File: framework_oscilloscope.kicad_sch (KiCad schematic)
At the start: 86 parts, among them IC1 FT232HL-REEL, IC10 93LC56BT-I_OT, IC2 ICE40UP5K-SG48I, IC3 ADC08060CIMTX_NOPB, IC7 OPA356AIDBVR, IC8 TLV77312PDBVR, IC9 LM4040C20IDBZT, J1 BNC, P1 USB_C_Plug_USB2.0, U9 TPS62A02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

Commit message: added part numbers for passives
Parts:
- C10, C12, C14, C15, C17, C18, C19, C21, C22, C26, C27, C29, C30, C31, C32, C33, C34, C39, C40, C43, C44, C46, C7, C8: MANUFACTURER PART NUMBER (none) -> CL05A105KO5NNNC
- C11, C13, C16, C20, C23, C9: MANUFACTURER PART NUMBER (none) -> CL10A475KP8NNNC
- C2: MANUFACTURER PART NUMBER (none) -> CC0402JRNPO9BN101
- C24: MANUFACTURER PART NUMBER (none) -> CC0402JRNPO9BN221
- C25, C47, C48, C49: MANUFACTURER PART NUMBER (none) -> CL05B104KO5NNNC
- C3, C35, C36, C37, C38, C4, C41, C42, C45, C5, C6: MANUFACTURER PART NUMBER (none) -> CL10A106MQ8NNNC
- R1: value 5.1k -> 5k1R; MANUFACTURER PART NUMBER (none) -> RC0402FR-075K1L
- R10: MANUFACTURER PART NUMBER (none) -> RT0402BRD074K12L
- R11: MANUFACTURER PART NUMBER (none) -> AT0402DRD073K32L
- R12, R13: MANUFACTURER PART NUMBER (none) -> RC0402FR-0775RL
- R14, R15, R16, R17, R18, R19, R7: MANUFACTURER PART NUMBER (none) -> RC0402JR-0710KL
- R2: MANUFACTURER PART NUMBER (none) -> ERA2AEB123X
- R3, R4: MANUFACTURER PART NUMBER (none) -> RC0402JR-072K2L
- R5: value 90.9kR -> 90k9R; MANUFACTURER PART NUMBER (none) -> RC0402FR-0790K9L
- R6: MANUFACTURER PART NUMBER (none) -> RC0402FR-0720KL
- R8: MANUFACTURER PART NUMBER (none) -> RC0402FR-07100RL
- R9: MANUFACTURER PART NUMBER (none) -> RT0402FRE071KL

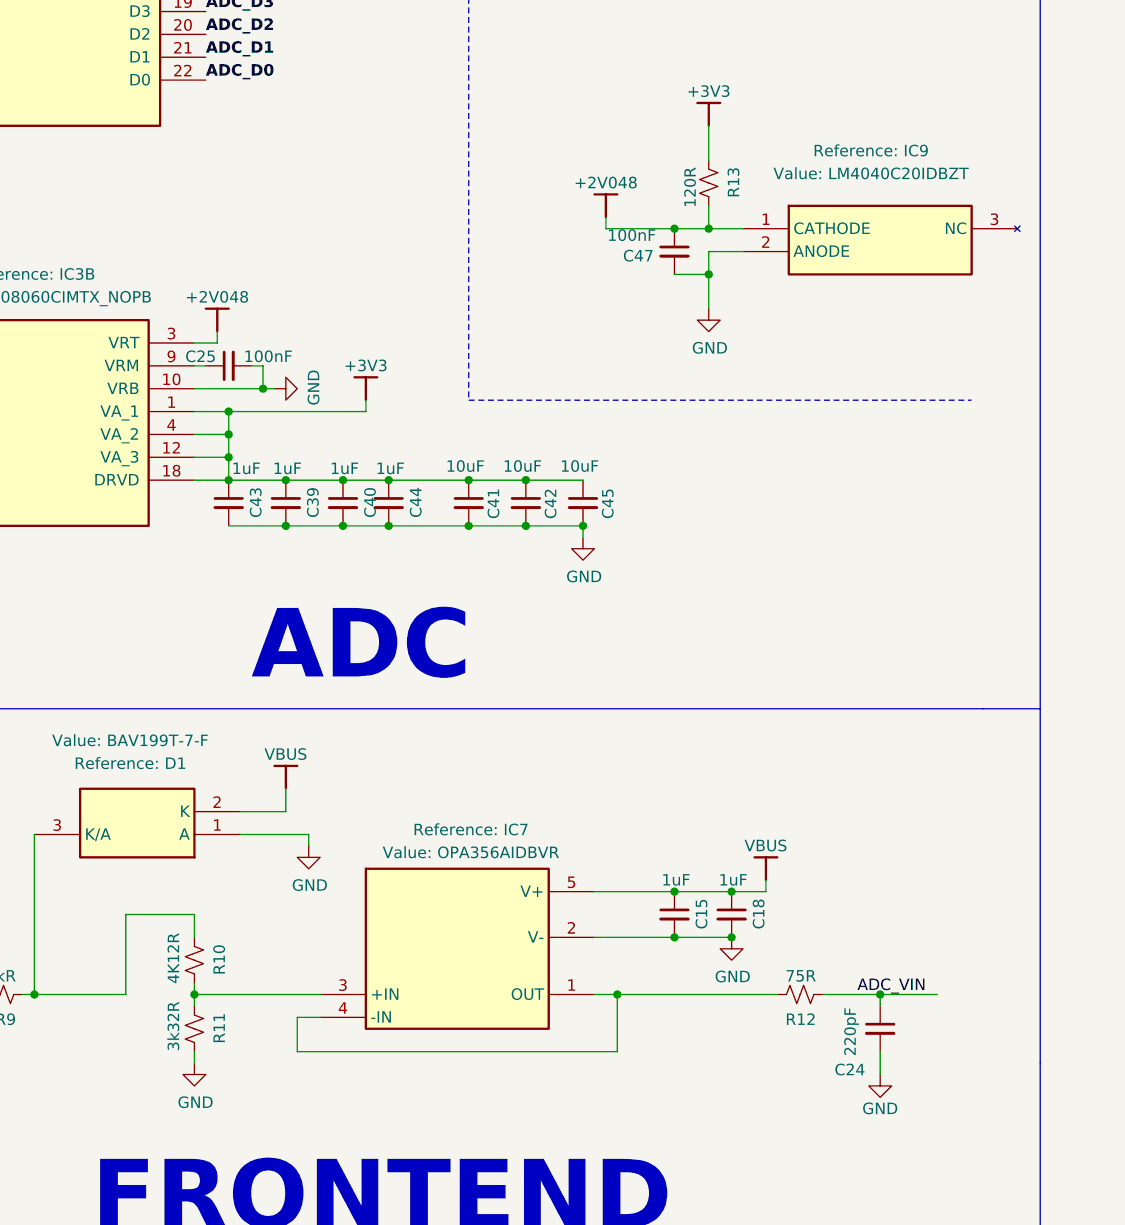
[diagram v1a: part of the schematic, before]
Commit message: improved dfm
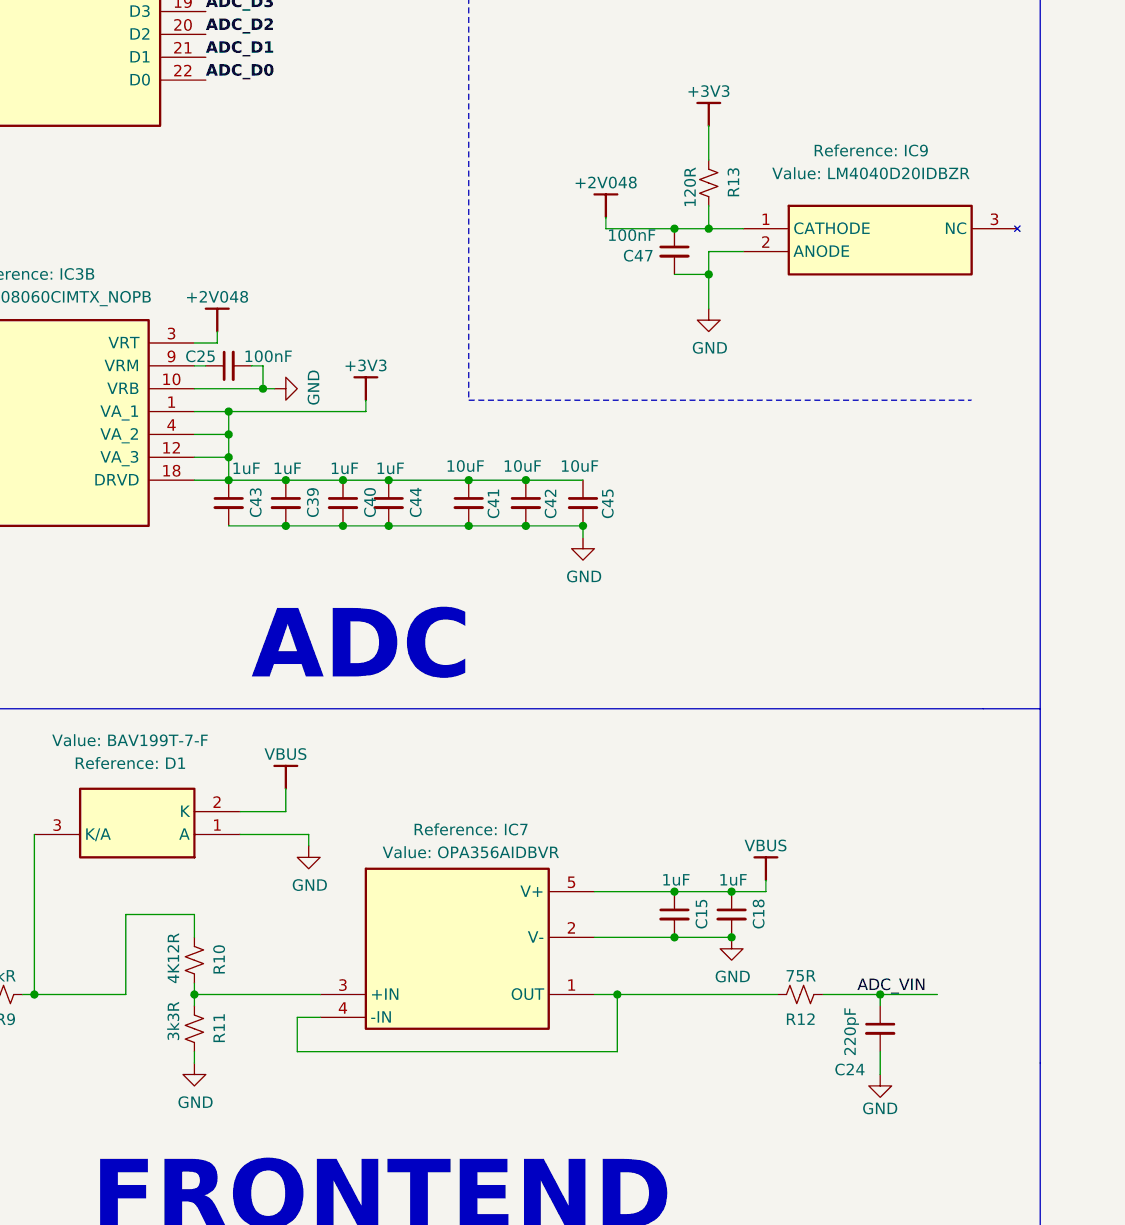
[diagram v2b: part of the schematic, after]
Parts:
- IC9: value LM4040C20IDBZT -> LM4040D20IDBZR; MANUFACTURER PART NUMBER LM4040C20IDBZT -> LM4040D20IDBZR
- R11: value 3k32R -> 3k3R; MANUFACTURER PART NUMBER AT0402DRD073K32L -> RT0402BRD073K3L
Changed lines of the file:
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@@
 			)
 		)
-		(property "Value" "3k32R"
+		(property "Value" "3k3R"
 			(at 188.214 236.982 90)
 			(show_name no)
@@
 			)
 		)
-		(property "MANUFACTURER PART NUMBER" "AT0402DRD073K32L"
+		(property "MANUFACTURER PART NUMBER" "RT0402BRD073K3L"
 			(at 190.5 240.03 0)
 			(hide yes)
@@
 			)
 		)
-		(property "Value" "LM4040C20IDBZT"
+		(property "Value" "LM4040D20IDBZR"
 			(at 265.684 145.034 0)
 			(show_name yes)
@@
 			)
 		)
-		(property "MANUFACTURER PART NUMBER" "LM4040C20IDBZT"
+		(property "MANUFACTURER PART NUMBER" "LM4040D20IDBZR"
 			(at 252.476 129.54 0)
 			(hide yes)
